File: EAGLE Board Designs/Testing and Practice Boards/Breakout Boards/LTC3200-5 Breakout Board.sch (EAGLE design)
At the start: 5 parts

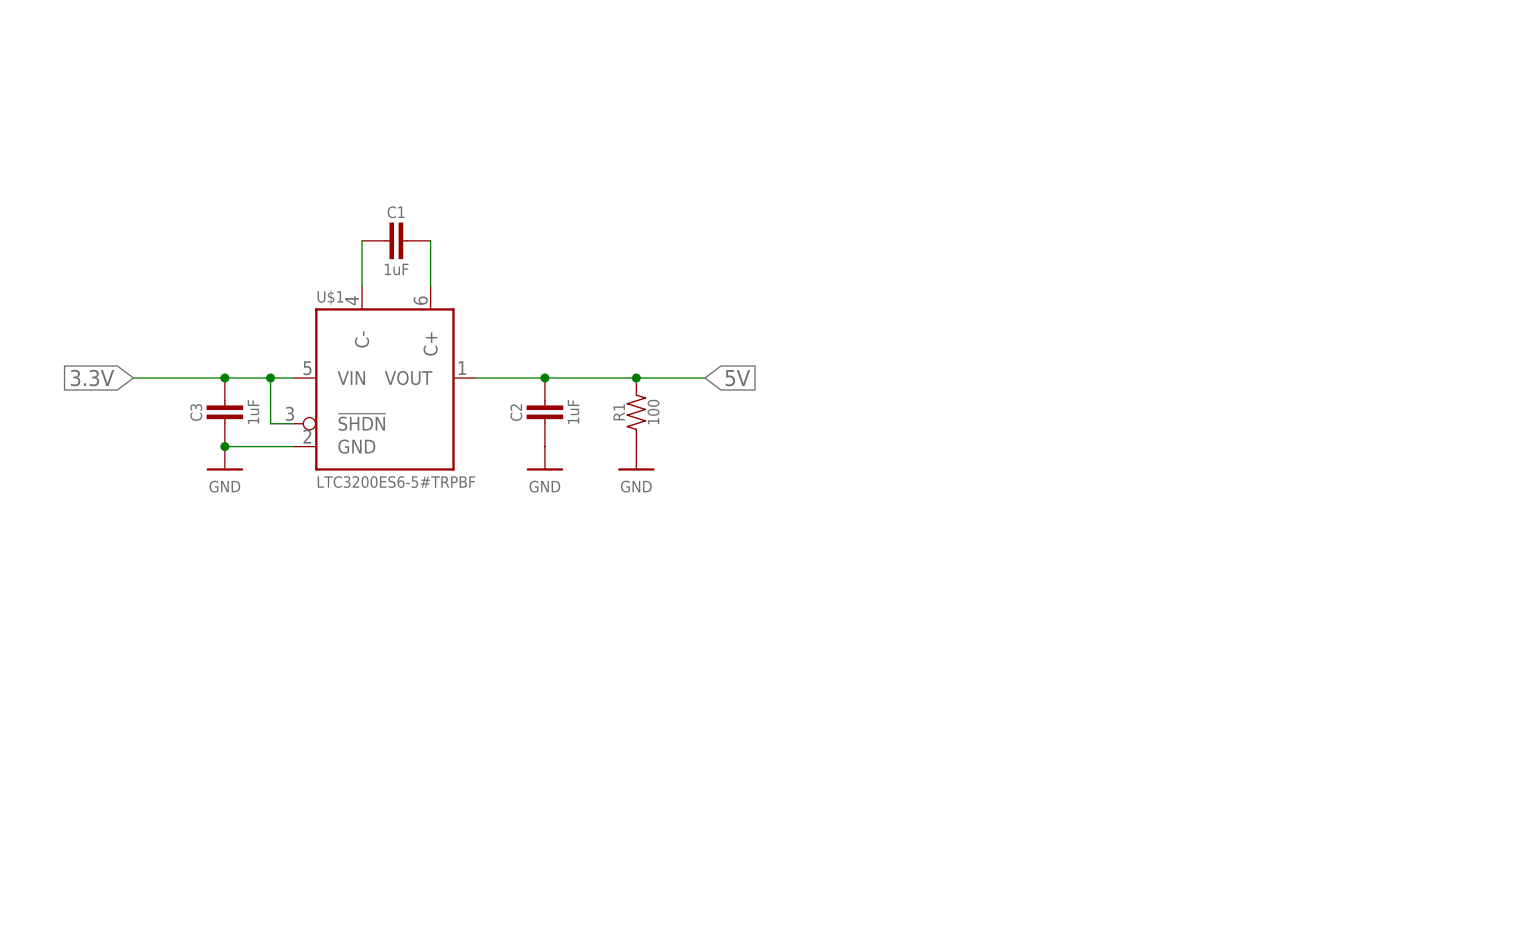
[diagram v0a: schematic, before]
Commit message: Added rest of circuitry
Added test points to connect wires to
Added jumper so you can measure current output (I recommend)
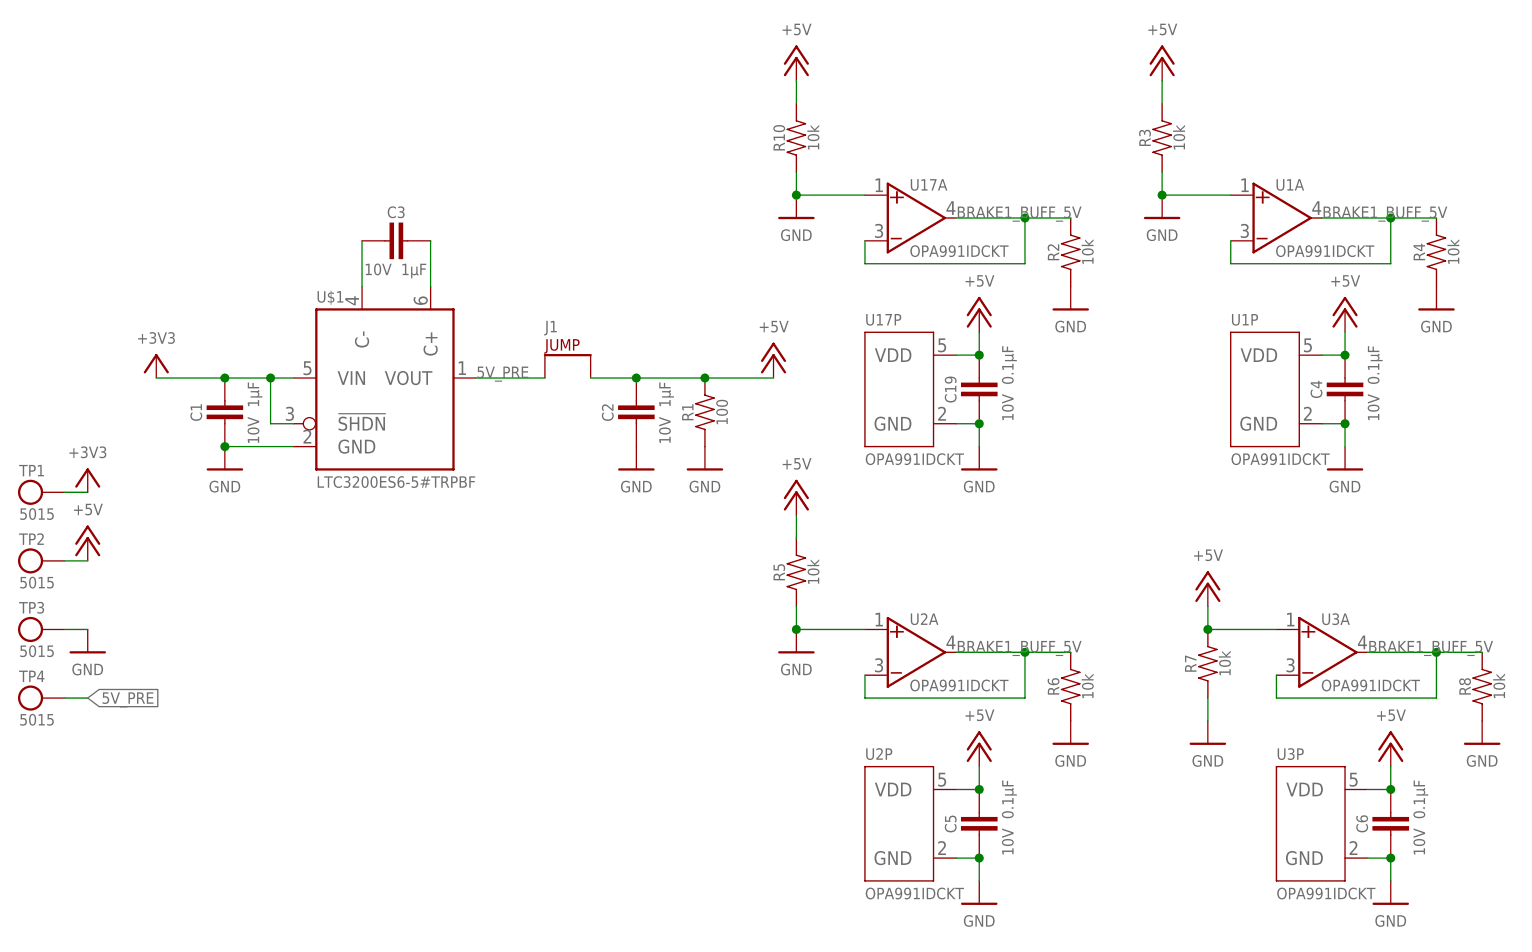
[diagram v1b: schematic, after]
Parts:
- added C19, C4, C5, C6: CAPACITOR_0603_10V_0.1UF, HyTechDevices:CAPACITOR_0603_10V_0.1UF
- added J1: JUMPER_1X02_, HyTechDevices:JUMPER_1X02_
- added R10, R2, R3, R4, R5, R6, R7, R8: RESISTOR_0603_10K, HyTechDevices:RESISTOR_0603_10K
- added TP1, TP2, TP3, TP4: TEST_POINT, HyTechDevices:TEST_POINT
- added U1, U17, U2, U3: OPAMP_1_CHANNEL_OPA991, HyTechDevices:OPAMP_1_CHANNEL_OPA991
- C1, C2, C3: value 1uF -> CAPACITOR_0603_10V_1UF; device HyTechDevices:CAPACITOR_VALUE -> HyTechDevices:CAPACITOR_0603_10V_1UF
- R1: value 100 -> RESISTOR_0603_100; device HyTechDevices:RESISTOR_VALUE -> HyTechDevices:RESISTOR_0603_100
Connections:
- removed net 3.3V: C3.1, U$1.!SHDN, U$1.VIN
- removed net 5V: C2.1, R1.2, U$1.VOUT
- new net +3V3: C1.1, TP1.P$1, U$1.!SHDN, U$1.VIN
- new net +5V: C19.1, C2.1, C4.1, C5.1, C6.1, J1.P$2, R1.2, R10.2, R3.2, R5.2, R7.2, TP2.P$1, U17P.VDD, U1P.VDD, U2P.VDD, U3A.VIN+, U3P.VDD
- new net 5V_PRE: J1.P$1, TP4.P$1, U$1.VOUT
- new net BRAKE1_BUFF_5V: R2.2, R4.2, R6.2, R8.2, U17A.VIN-, U17A.VOUT, U1A.VIN-, U1A.VOUT, U2A.VIN-, U2A.VOUT, U3A.VIN-, U3A.VOUT
- net GND: now also C1.2, C19.2, C4.2, C5.2, C6.2, R10.1, R2.1, R3.1, R4.1, R5.1, R6.1, R7.1, R8.1, TP3.P$1, U17A.VIN+, U17P.GND, U1A.VIN+, U1P.GND, U2A.VIN+, U2P.GND, U3P.GND; no longer C3.2
- net N$3: now also C3.2; no longer C1.2
- net N$4: now also C3.1; no longer C1.1
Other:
- moved on the sheet: C1, C2, C3, R1
